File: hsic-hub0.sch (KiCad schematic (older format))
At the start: 17 parts, among them J16 SM05B-SRSS-TB, J17 SM05B-SRSS-TB, U11 USB3503, U12 TPS2054D, X2 ASTXR-12

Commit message: Major commit. Work in progress on board layout.
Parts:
- renumbered U12 to U10
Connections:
- net 5V: now also U10.6 (IN2); no longer U10.2 (IN1)
- net GND: now also U10.5 (GND); no longer U10.1 (GND)
- net PRTPWR: now also U10.7 (EN3), U10.8 (EN4); no longer U10.3 (EN1), U10.4 (EN2)
- net USB1_5V: now also U10.11 (OUT3); no longer U10.15 (OUT1)
- net USB2_5V: now also U10.10 (OUT4); no longer U10.14 (OUT2)
- net ~OSC: now also U10.12 (~OC3), U10.9 (~OC4); no longer U10.13 (~OC2), U10.16 (~OC1)
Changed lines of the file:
@@
 ~OSC
 $Comp
-L Drone:TPS2054D U12
-U 1 1 5E4E09E8
+L Drone:TPS2054D U10
+U 2 1 5E4E09E8
 P 8550 3150
-AR Path="/5E2EDC4D/5E4E09E8" Ref="U12"  Part="1"
+AR Path="/5E2EDC4D/5E4E09E8" Ref="U10"  Part="2"
 AR Path="/5E349830/5E4E09E8" Ref="U?"  Part="1"
-F 0 "U12" H 8250 3300 50  0000 L BNN
+F 0 "U10" H 8250 3300 50  0000 L BNN
 F 1 "TPS2054D" H 8250 3200 50  0000 L BNN
 F 2 "Package_SO:SOIC-16_3.9x9.9mm_P1.27mm" H 8250 3400 50  0001 L BNN
 F 3 "" H 8500 3150 50  0001 C CNN
-	1    8550 3150
+	2    8550 3150
 	1    0    0    -1
 $EndComp

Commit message: Work in progress on laying out the board.
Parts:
- C43, C44, C45, C46, C47, C48, C49, C50, C51: footprint Capacitor_SMD:C_0805_2012Metric -> Drone:C0805
- R42, R43, R44: footprint Resistor_SMD:R_0805_2012Metric -> Drone:R0805
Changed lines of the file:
@@
 F 0 "C43" H 1265 5046 50  0000 L CNN
 F 1 "100n" H 1265 4955 50  0000 L CNN
-F 2 "Capacitor_SMD:C_0805_2012Metric" H 1188 4850 50  0001 C CNN
+F 2 "Drone:C0805" H 1188 4850 50  0001 C CNN
 F 3 "~" H 1150 5000 50  0001 C CNN
 	1    1150 5000
@@
 F 0 "C50" H 9715 3546 50  0000 L CNN
 F 1 "100n" H 9715 3455 50  0000 L CNN
-F 2 "Capacitor_SMD:C_0805_2012Metric" H 9638 3350 50  0001 C CNN
+F 2 "Drone:C0805" H 9638 3350 50  0001 C CNN
 F 3 "~" H 9600 3500 50  0001 C CNN
 	1    9600 3500
@@
 F 0 "C45" H 2515 5046 50  0000 L CNN
 F 1 "1n" H 2515 4955 50  0000 L CNN
-F 2 "Capacitor_SMD:C_0805_2012Metric" H 2438 4850 50  0001 C CNN
+F 2 "Drone:C0805" H 2438 4850 50  0001 C CNN
 F 3 "~" H 2400 5000 50  0001 C CNN
 	1    2400 5000
@@
 F 0 "C48" H 9515 1396 50  0000 L CNN
 F 1 "100n" H 9515 1305 50  0000 L CNN
-F 2 "Capacitor_SMD:C_0805_2012Metric" H 9438 1200 50  0001 C CNN
+F 2 "Drone:C0805" H 9438 1200 50  0001 C CNN
 F 3 "~" H 9400 1350 50  0001 C CNN
 	1    9400 1350
@@
 F 0 "C49" H 9515 2396 50  0000 L CNN
 F 1 "100n" H 9515 2305 50  0000 L CNN
-F 2 "Capacitor_SMD:C_0805_2012Metric" H 9438 2200 50  0001 C CNN
+F 2 "Drone:C0805" H 9438 2200 50  0001 C CNN
 F 3 "~" H 9400 2350 50  0001 C CNN
 	1    9400 2350
@@
 F 0 "R44" H 7070 1646 50  0000 L CNN
 F 1 "10k" H 7070 1555 50  0000 L CNN
-F 2 "Resistor_SMD:R_0805_2012Metric" V 6930 1600 50  0001 C CNN
+F 2 "Drone:R0805" V 6930 1600 50  0001 C CNN
 F 3 "~" H 7000 1600 50  0001 C CNN
 	1    7000 1600
@@
 F 0 "C51" H 10165 3546 50  0000 L CNN
 F 1 "10u" H 10165 3455 50  0000 L CNN
-F 2 "Capacitor_SMD:C_0805_2012Metric" H 10088 3350 50  0001 C CNN
+F 2 "Drone:C0805" H 10088 3350 50  0001 C CNN
 F 3 "~" H 10050 3500 50  0001 C CNN
 	1    10050 3500
@@
 F 0 "C46" H 2865 3596 50  0000 L CNN
 F 1 "4u7" H 2865 3505 50  0000 L CNN
-F 2 "Capacitor_SMD:C_0805_2012Metric" H 2788 3400 50  0001 C CNN
+F 2 "Drone:C0805" H 2788 3400 50  0001 C CNN
 F 3 "~" H 2750 3550 50  0001 C CNN
 	1    2750 3550
@@
 F 0 "C47" H 3265 3596 50  0000 L CNN
 F 1 "1u" H 3265 3505 50  0000 L CNN
-F 2 "Capacitor_SMD:C_0805_2012Metric" H 3188 3400 50  0001 C CNN
+F 2 "Drone:C0805" H 3188 3400 50  0001 C CNN
 F 3 "~" H 3150 3550 50  0001 C CNN
 	1    3150 3550
@@
 F 0 "R43" H 4270 3596 50  0000 L CNN
 F 1 "12k,1%" H 4270 3505 50  0000 L CNN
-F 2 "Resistor_SMD:R_0805_2012Metric" V 4130 3550 50  0001 C CNN
+F 2 "Drone:R0805" V 4130 3550 50  0001 C CNN
 F 3 "~" H 4200 3550 50  0001 C CNN
 	1    4200 3550
@@
 F 0 "R42" H 2570 3096 50  0000 L CNN
 F 1 "DNP" H 2570 3005 50  0000 L CNN
-F 2 "Resistor_SMD:R_0805_2012Metric" V 2430 3050 50  0001 C CNN
+F 2 "Drone:R0805" V 2430 3050 50  0001 C CNN
 F 3 "~" H 2500 3050 50  0001 C CNN
 	1    2500 3050
@@
 F 0 "C44" H 2415 3596 50  0000 L CNN
 F 1 "100n" H 2415 3505 50  0000 L CNN
-F 2 "Capacitor_SMD:C_0805_2012Metric" H 2338 3400 50  0001 C CNN
+F 2 "Drone:C0805" H 2338 3400 50  0001 C CNN
 F 3 "~" H 2300 3550 50  0001 C CNN
 	1    2300 3550

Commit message: Many the minor updates.
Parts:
- added R37: 10k, Drone:R0805, symbol Drone:RES
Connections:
- net PRTPWR: now also R44.2
- net VDD33_BYP: now also R37.1
- net ~OSC: now also R37.2; no longer R44.2
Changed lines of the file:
@@
 Text Label 10450 3250 2    50   ~ 0
 5V
-Wire Wire Line
-	6000 1900 6700 1900
 $Comp
 L Drone:CAP C50
@@
 Wire Wire Line
 	7000 1000 7000 1450
-Wire Wire Line
-	6000 2050 7000 2050
 $Comp
 L Drone:RES R44
@@
 	1    0    0    -1
 $EndComp
-Wire Wire Line
-	7000 2050 7000 1750
 $Comp
 L Drone:SM05B-SRSS-TB J16
@@
 Text Label 2300 4100 1    50   ~ 0
 GND
+Wire Wire Line
+	7300 1000 7300 1450
+$Comp
+L Drone:RES R37
+U 1 1 5E58C868
+P 7300 1600
+AR Path="/5E2EDC4D/5E58C868" Ref="R37"  Part="1"
+AR Path="/5E349830/5E58C868" Ref="R?"  Part="1"
+F 0 "R37" H 7370 1646 50  0000 L CNN
+F 1 "10k" H 7370 1555 50  0000 L CNN
+F 2 "Drone:R0805" V 7230 1600 50  0001 C CNN
+F 3 "~" H 7300 1600 50  0001 C CNN
+	1    7300 1600
+	1    0    0    -1
+$EndComp
+Text Label 7300 1000 3    50   ~ 0
+VDD33_BYP
+Wire Wire Line
+	7300 2050 7300 1750
+Wire Wire Line
+	6000 2050 7300 2050
+Wire Wire Line
+	7000 1900 7000 1750
+Wire Wire Line
+	6000 1900 7000 1900
 $EndSCHEMATC

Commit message: Update layout
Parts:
- U10: footprint Package_SO:SOIC-16_3.9x9.9mm_P1.27mm -> Drone:TPS2054D
- renumbered J16 to J4, J17 to J8
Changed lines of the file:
@@
 F 0 "U10" H 8250 3300 50  0000 L BNN
 F 1 "TPS2054D" H 8250 3200 50  0000 L BNN
-F 2 "Package_SO:SOIC-16_3.9x9.9mm_P1.27mm" H 8250 3400 50  0001 L BNN
+F 2 "Drone:TPS2054D" H 8250 3400 50  0001 L BNN
 F 3 "" H 8500 3150 50  0001 C CNN
 	2    8550 3150
@@
 $EndComp
 $Comp
-L Drone:SM05B-SRSS-TB J16
+L Drone:SM05B-SRSS-TB J4
 U 1 1 5E385FFC
 P 8500 1100
-AR Path="/5E2EDC4D/5E385FFC" Ref="J16"  Part="1"
+AR Path="/5E2EDC4D/5E385FFC" Ref="J4"  Part="1"
 AR Path="/5E349830/5E385FFC" Ref="J?"  Part="1"
-F 0 "J16" H 8475 1000 50  0000 R CNN
+F 0 "J4" H 8475 1000 50  0000 R CNN
 F 1 "SM05B-SRSS-TB" H 8475 1075 50  0000 R CNN
 F 2 "Drone:SM05B-SRSS-TB" H 8350 1350 50  0001 L CNN
@@
 $EndComp
 $Comp
-L Drone:SM05B-SRSS-TB J17
+L Drone:SM05B-SRSS-TB J8
 U 1 1 5E3AC9C2
 P 8500 2100
-AR Path="/5E2EDC4D/5E3AC9C2" Ref="J17"  Part="1"
+AR Path="/5E2EDC4D/5E3AC9C2" Ref="J8"  Part="1"
 AR Path="/5E349830/5E3AC9C2" Ref="J?"  Part="1"
-F 0 "J17" H 8475 2000 50  0000 R CNN
+F 0 "J8" H 8475 2000 50  0000 R CNN
 F 1 "SM05B-SRSS-TB" H 8475 2075 50  0000 R CNN
 F 2 "Drone:SM05B-SRSS-TB" H 8350 2350 50  0001 L CNN

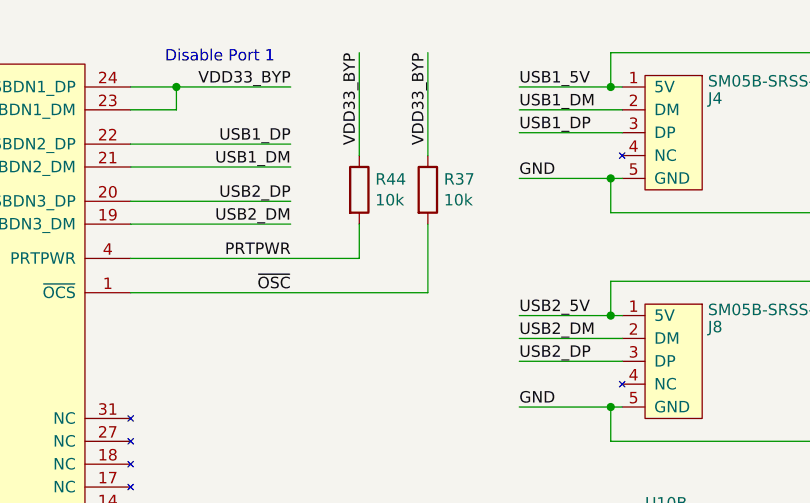
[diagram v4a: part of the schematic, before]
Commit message: Use standard names for differential pair nets.
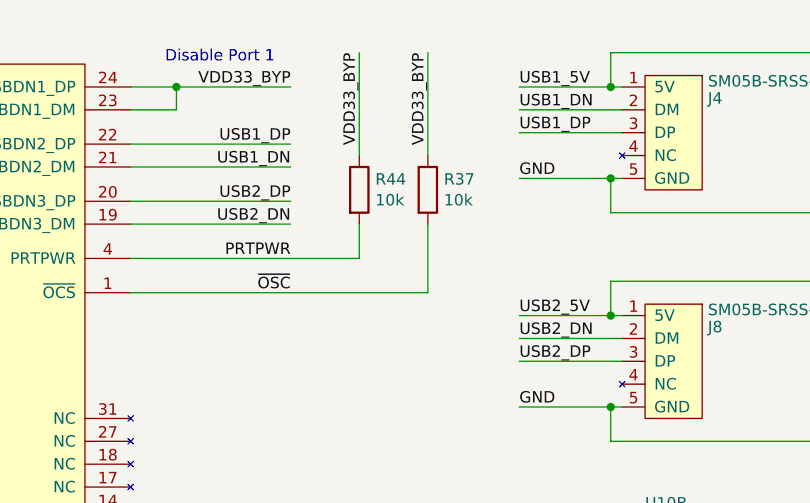
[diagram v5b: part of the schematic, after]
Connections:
- net USB1_DM renamed USB1_DN
- net USB2_DM renamed USB2_DN
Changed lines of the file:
@@
 	9050 3550 9400 3550
 Text Label 7700 1250 0    50   ~ 0
-USB1_DM
+USB1_DN
 Text Label 7700 1350 0    50   ~ 0
 USB1_DP
@@
 $EndComp
 Text Label 7700 2250 0    50   ~ 0
-USB2_DM
+USB2_DN
 Text Label 7700 2350 0    50   ~ 0
 USB2_DP
@@
 	8100 2700 8100 2550
 Text Label 6700 1500 2    50   ~ 0
-USB1_DM
+USB1_DN
 Text Label 6700 1400 2    50   ~ 0
 USB1_DP
@@
 	6000 1500 6700 1500
 Text Label 6700 1750 2    50   ~ 0
-USB2_DM
+USB2_DN
 Text Label 6700 1650 2    50   ~ 0
 USB2_DP

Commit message: Major commit 1. Moved a couple components and rerouted accordingly 2. Added fabrication information to all components 3. Several clean ups to footprints 4. Removed some unused components
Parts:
- U10: value TPS2054D -> TPS2054BDR; footprint Drone:TPS2054D -> Drone:TPS2054BDR; symbol Drone:TPS2054D -> Drone:TPS2054BDR
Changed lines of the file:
@@
 ~OSC
 $Comp
-L Drone:TPS2054D U10
+L Drone:TPS2054BDR U10
 U 2 1 5E4E09E8
 P 8550 3150
 AR Path="/5E2EDC4D/5E4E09E8" Ref="U10"  Part="2"
 AR Path="/5E349830/5E4E09E8" Ref="U?"  Part="1"
+AR Path="/5E4E09E8" Ref="U10"  Part="2"
 F 0 "U10" H 8250 3300 50  0000 L BNN
-F 1 "TPS2054D" H 8250 3200 50  0000 L BNN
-F 2 "Drone:TPS2054D" H 8250 3400 50  0001 L BNN
+F 1 "TPS2054BDR" H 8250 3200 50  0000 L BNN
+F 2 "Drone:TPS2054BDR" H 8250 3400 50  0001 L BNN
 F 3 "" H 8500 3150 50  0001 C CNN
 	2    8550 3150
